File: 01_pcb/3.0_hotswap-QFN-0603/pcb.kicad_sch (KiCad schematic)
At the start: 126 parts, among them J1 TYPE-C-31-M12_13, J2 AVR-ISP-6_mod, J3 4PIN, J5 Conn_01x08, SW1 SW_PUSH, U1 ATmega32U4-M, U4 USBLC6-2SC6, Y1 16MHz

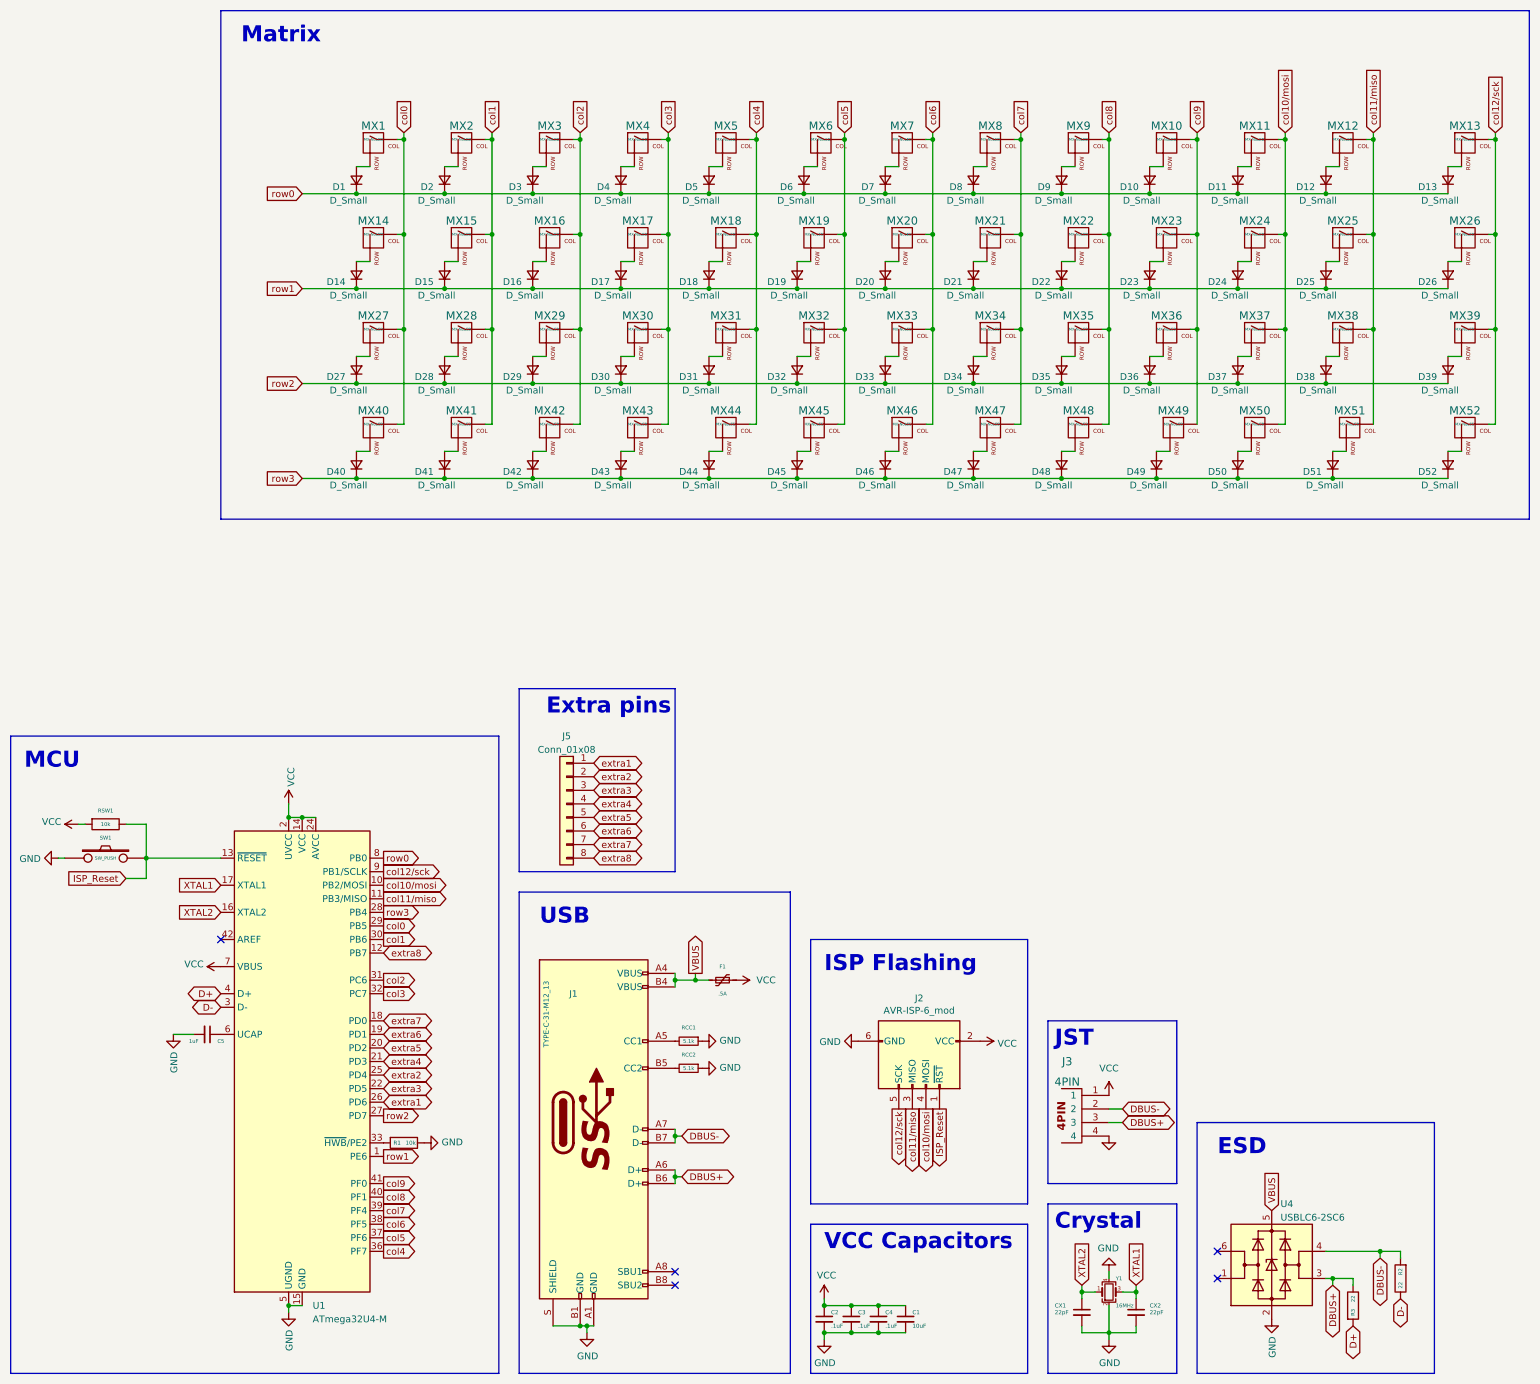
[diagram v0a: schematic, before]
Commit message: updated QFN, removed some vias
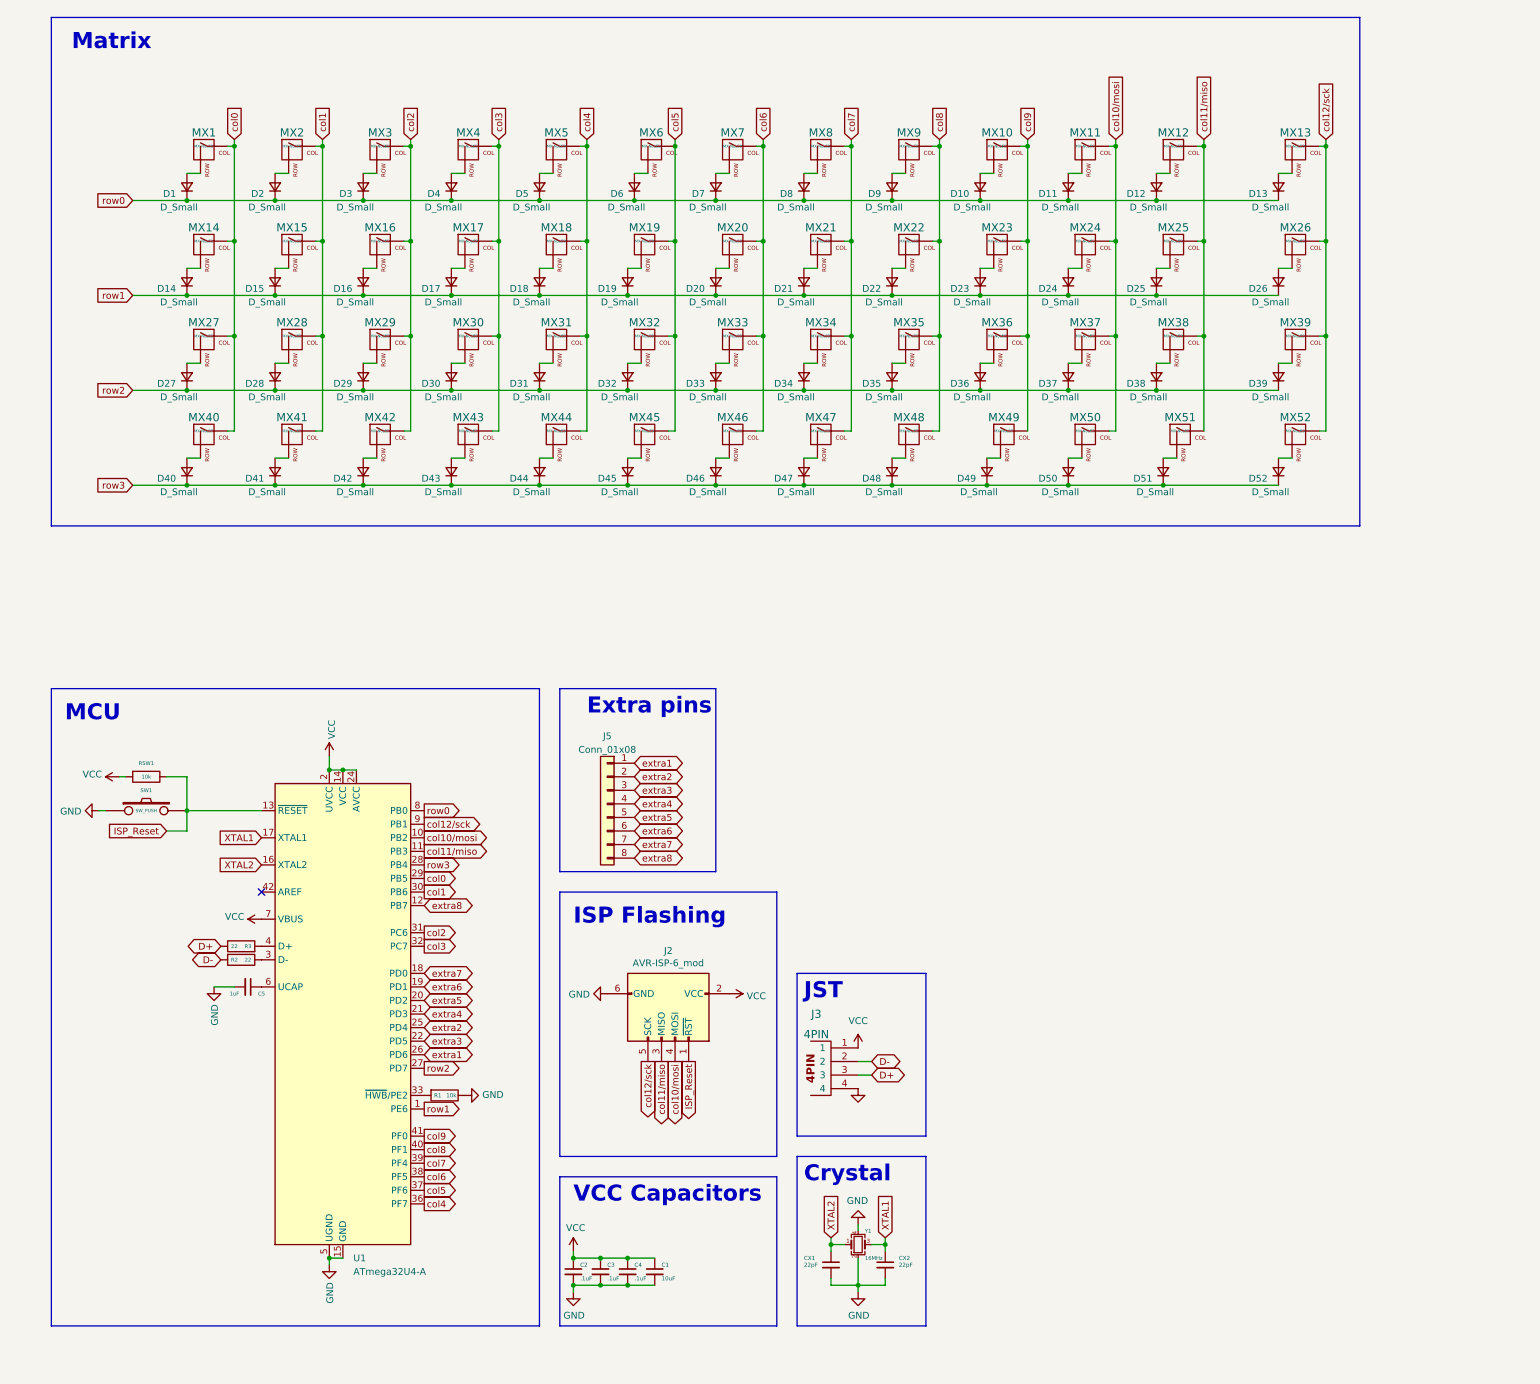
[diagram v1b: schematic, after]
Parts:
- removed F1: .5A, Fuse:Fuse_0805_2012Metric_Pad1.15x1.40mm_HandSolder, symbol Device:Polyfuse_Small
- removed J1: TYPE-C-31-M12_13, acheron_Connectors:TYPE-C-31-M-12, symbol pcb-rescue:TYPE-C-31-M12_13-acheronSymbols-Ori-rescue-lucy-rescue
- removed RCC1, RCC2: 5.1k, Resistor_SMD:R_0603_1608Metric, symbol Device:R_Small
- removed U1: ATmega32U4-M, Package_DFN_QFN:QFN-44-1EP_7x7mm_P0.5mm_EP5.2x5.2mm, symbol MCU_Microchip_ATmega:ATmega32U4-M
- removed U4: USBLC6-2SC6, marbastlib-various:SOT-23-6-routable, symbol Power_Protection:USBLC6-2SC6
- added U1: ATmega32U4-A, Package_DFN_QFN:QFN-44-1EP_7x7mm_P0.5mm_EP5.2x5.2mm, symbol MCU_Microchip_ATmega:ATmega32U4-A
- MX1, MX10, MX11, MX12, MX13, MX14, MX15, MX16, MX17, MX18, MX19, MX2, MX20, MX21, MX22, MX23, MX24, MX25, MX26, MX27, MX28, MX29, MX3, MX30, MX31, MX32, MX33, MX34, MX35, MX36, MX37, MX38, MX39, MX4, MX40, MX41, MX42, MX43, MX44, MX45, MX46, MX47, MX48, MX49, MX5, MX50, MX51, MX52, MX6, MX7, MX8, MX9: footprint MX_Only:MXOnly-1U-Hotswap -> marbastlib-mx:SW_MX_HS_S_1u
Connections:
- net DBUS+ is gone; now on net D+: J3.3, R3.1
- net DBUS- is gone; now on net D-: J3.2, R2.2
- net D+: no longer R3.2
- net D-: no longer R2.1
- net GND: now also U1.15 (GND), U1.23 (GND), U1.35 (GND), U1.43 (GND), U1.5 (UGND)
- net ISP_Reset: now also U1.13 (~{RESET})
- net VCC: now also U1.14 (VCC), U1.2 (UVCC), U1.24 (AVCC), U1.34 (VCC), U1.44 (AVCC), U1.7 (VBUS)
- net XTAL1: now also U1.17 (XTAL1)
- net XTAL2: now also U1.16 (XTAL2)
- net col0: now also U1.29 (PB5)
- net col1: now also U1.30 (PB6)
- net col10/mosi: now also U1.10 (PB2)
- net col11/miso: now also U1.11 (PB3)
- net col12/sck: now also U1.9 (PB1)
- net col2: now also U1.31 (PC6)
- net col3: now also U1.32 (PC7)
- net col4: now also U1.36 (PF7)
- net col5: now also U1.37 (PF6)
- net col6: now also U1.38 (PF5)
- net col7: now also U1.39 (PF4)
- net col8: now also U1.40 (PF1)
- net col9: now also U1.41 (PF0)
- net extra1: now also U1.26 (PD6)
- net extra2: now also U1.25 (PD4)
- net extra3: now also U1.22 (PD5)
- net extra4: now also U1.21 (PD3)
- net extra5: now also U1.20 (PD2)
- net extra6: now also U1.19 (PD1)
- net extra7: now also U1.18 (PD0)
- net extra8: now also U1.12 (PB7)
- net row0: now also U1.8 (PB0)
- net row1: now also U1.1 (PE6)
- net row2: now also U1.27 (PD7)
- net row3: now also U1.28 (PB4)
- net at R1.2: now also U1.33 (~{HWB}/PE2)
- net at C5.1: now also U1.6 (UCAP)
- new net: R3.2, U1.4 (D+)
- new net: R2.1, U1.3 (D-)
- no-connect marks 5 -> 1
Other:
- note removed: "ESD"
- note removed: "USB"
- moved on the sheet: C1, C2, C3, C4, C5, CX1, CX2, D1, D10, D11, D12, D13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
